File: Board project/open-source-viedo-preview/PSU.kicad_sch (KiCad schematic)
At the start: 33 parts

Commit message: Imporoved electrical schematic
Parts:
- J14: renamed from J?; footprint (none) -> TerminalBlock_Phoenix:TerminalBlock_Phoenix_MKDS-1,5-2_1x02_P5.00mm_Horizontal
- gave numbers to parts that had none: 32
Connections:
- net +12V: no longer J15.1 (Pin_1)
- net +5V: no longer J15.4 (Pin_4)
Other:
- moved on the sheet: C12, C14, C7, D3, J14, Q2, R9, TP1

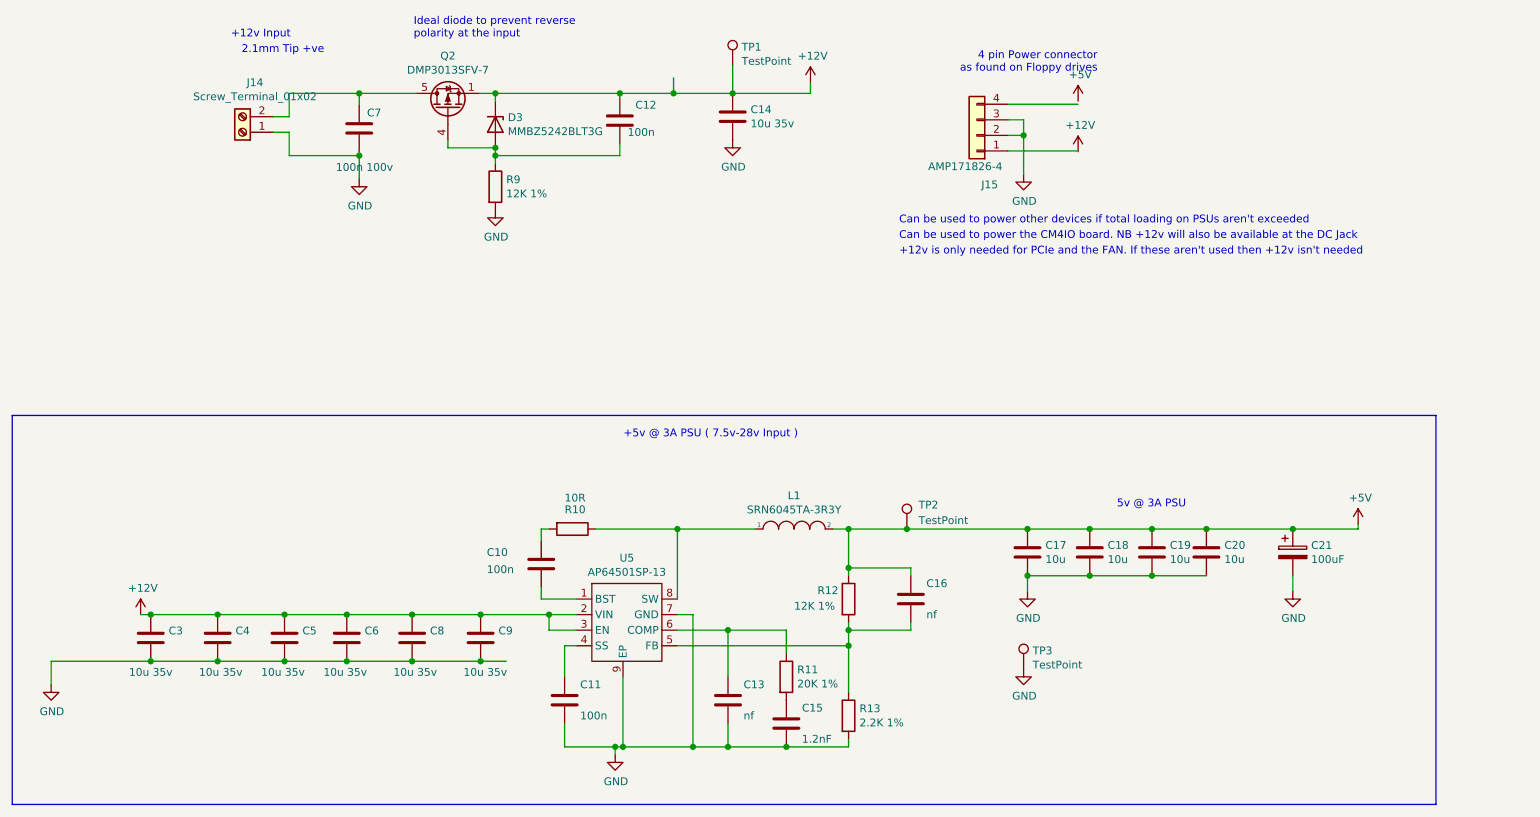
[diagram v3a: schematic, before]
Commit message: ERC error repaired
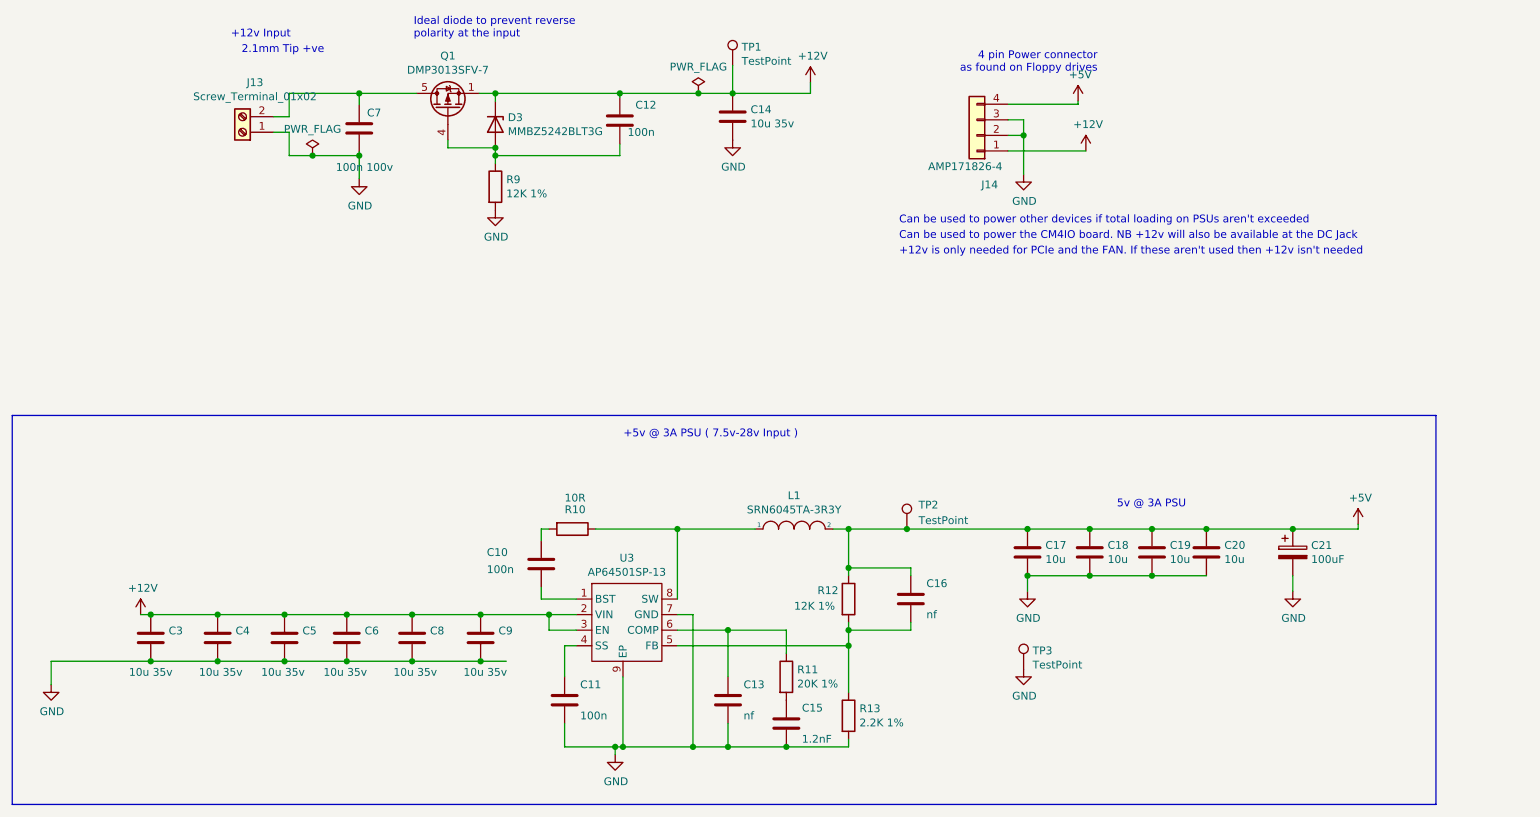
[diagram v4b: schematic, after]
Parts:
- renumbered J14 to J13, J15 to J14, Q2 to Q1, U5 to U3
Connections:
- net +12V: now also J14.1 (Pin_1)
- net +5V: now also J14.4 (Pin_4)
